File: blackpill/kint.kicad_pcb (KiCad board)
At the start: 2 copper layers, 99.9 x 86 mm, 17 parts, among them J1 RIGHT_THUMB, J2 LEFT_KEYWELL, J3 LEFT_FN_KEYS, J4 RIGHT_FN_KEYS, J7 RIGHT_KEYWELL, J8 LEFT_THUMB, U1 YAAJ_WeAct_BlackPill_Part_Lik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

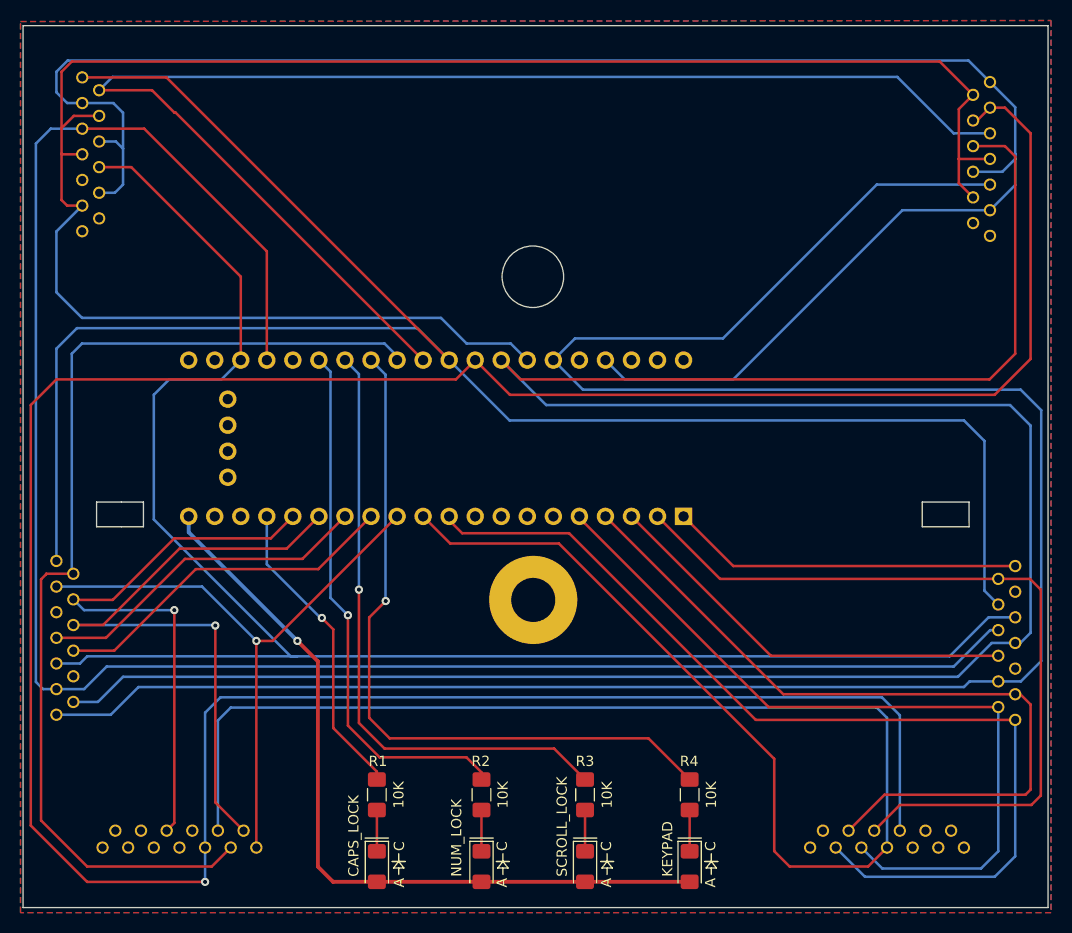
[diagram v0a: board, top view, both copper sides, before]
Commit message: Remove silkscreen writing area
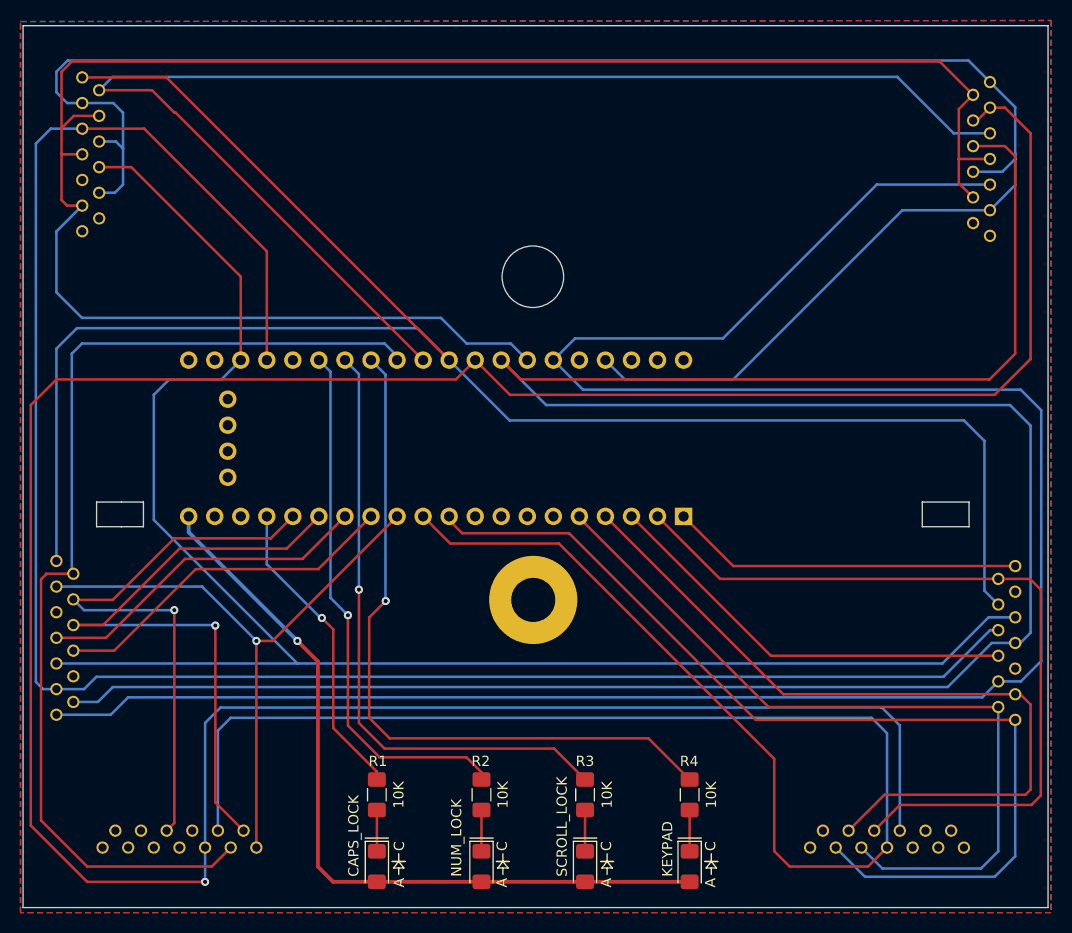
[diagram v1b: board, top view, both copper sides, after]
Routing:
- net /COL_6: track 155.0 -> 152.7 mm
- net /COL_5: track 288.1 -> 286.1 mm

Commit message: move tracks
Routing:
- net /LED_KEYPAD: track 69.9 -> 66.8 mm
- net /LED_SCROLL_LOCK: track 60.3 -> 58.8 mm
- net /ROW_3: track 56.8 -> 58.1 mm
- net /LED_NUM_LOCK: track 52.4 -> 51.9 mm
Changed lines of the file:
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@@
-	)
-	(segment
-		(start 113.5 119)
-		(end 113.5 139.75)
-		(width 0.25)
-		(layer "F.Cu")
-		(net 2)
 	)
 	(segment
@@
 	)
 	(segment
+		(start 114 139.25)
+		(end 112.75 140.5)
+		(width 0.25)
+		(layer "F.Cu")
+		(net 2)
+	)
+	(segment
 		(start 125.06 109.855)
 		(end 122.915 112)
@@
 	)
 	(segment
-		(start 113.5 139.75)
-		(end 112.75 140.5)
+		(start 114 118)
+		(end 114 139.25)
 		(width 0.25)
 		(layer "F.Cu")
@@
 	)
 	(via
-		(at 113.5 119)
+		(at 114 118)
 		(size 0.8)
 		(drill 0.4)
@@
 	)
 	(segment
-		(start 113.5 119)
-		(end 104.7 119)
-		(width 0.25)
-		(layer "B.Cu")
-		(net 2)
-	)
-	(segment
-		(start 104.7 119)
-		(end 103.65 117.95)
+		(start 114 118)
+		(end 103.7 118)
 		(width 0.25)
 		(layer "B.Cu")
@@
 	)
 	(segment
-		(start 107.642834 122.95)
+		(start 115 115)
+		(end 107.05 122.95)
+		(width 0.25)
+		(layer "F.Cu")
+		(net 22)
+	)
+	(segment
+		(start 127.535 115)
+		(end 115 115)
+		(width 0.25)
+		(layer "F.Cu")
+		(net 22)
+	)
+	(segment
+		(start 107.05 122.95)
 		(end 103.65 122.95)
 		(width 0.25)
@@
 	)
 	(segment
-		(start 127.535 115)
-		(end 115.592834 115)
-		(width 0.25)
-		(layer "F.Cu")
-		(net 22)
-	)
-	(segment
-		(start 115.592834 115)
-		(end 107.642834 122.95)
-		(width 0.25)
-		(layer "F.Cu")
-		(net 22)
-	)
-	(segment
-		(start 125.5 122)
-		(end 127.5 124)
-		(width 0.375)
-		(layer "F.Cu")
-		(net 24)
-	)
-	(segment
-		(start 127.5 144.01)
-		(end 128.9811 145.4911)
-		(width 0.375)
-		(layer "F.Cu")
-		(net 24)
-	)
-	(segment
-		(start 127.5 124)
-		(end 127.5 144.01)
+		(start 126 122.5)
+		(end 126 142.51)
 		(width 0.375)
 		(layer "F.Cu")
@@
 		(net 24)
 	)
+	(segment
+		(start 126 142.51)
+		(end 128.9811 145.4911)
+		(width 0.375)
+		(layer "F.Cu")
+		(net 24)
+	)
 	(via
-		(at 125.5 122)
+		(at 126 122.5)
 		(size 0.8)
 		(drill 0.4)
@@
 	)
 	(segment
+		(start 126 122.5)
+		(end 114.9 111.4)
+		(width 0.375)
+		(layer "B.Cu")
+		(net 24)
+	)
+	(segment
 		(start 114.9 111.4)
 		(end 114.9 109.855)
@@
 	)
 	(segment
-		(start 125.5 122)
-		(end 114.9 111.4)
-		(width 0.375)
-		(layer "B.Cu")
-		(net 24)
-	)
-	(segment
 		(start 158.08 109.855)
 		(end 171.675 123.45)
@@
 	)
 	(segment
-		(start 195.5 119.7)
-		(end 192.906544 119.7)
+		(start 192.3 119.7)
+		(end 195.5 119.7)
+		(width 0.25)
+		(layer "B.Cu")
+		(net 35)
+	)
+	(segment
+		(start 125.5 124.2)
+		(end 187.8 124.2)
 		(width 0.25)
 		(layer "B.Cu")
@@
 	)
 	(segment
-		(start 188.406544 124.2)
-		(end 125.5 124.2)
+		(start 187.8 124.2)
+		(end 192.3 119.7)
 		(width 0.25)
 		(layer "B.Cu")
@@
 		(start 111.5 98)
 		(end 111.5 110.2)
-		(width 0.25)
-		(layer "B.Cu")
-		(net 35)
-	)
-	(segment
-		(start 192.906544 119.7)
-		(end 188.406544 124.2)
 		(width 0.25)
 		(layer "B.Cu")
@@
 	)
 	(segment
-		(start 129 120.872)
-		(end 129 130.5)
-		(width 0.25)
-		(layer "F.Cu")
-		(net 48)
-	)
-	(segment
-		(start 129 130.5)
-		(end 133.2511 134.7511)
+		(start 127.25 120.25)
+		(end 127.25 128.75)
 		(width 0.25)
 		(layer "F.Cu")
@@
 	)
 	(segment
-		(start 127.889 119.761)
-		(end 129 120.872)
+		(start 127.25 128.75)
+		(end 133.2511 134.7511)
 		(width 0.25)
 		(layer "F.Cu")
@@
 	)
 	(via
-		(at 127.889 119.761)
+		(at 127.25 120.25)
 		(size 0.8)
 		(drill 0.4)
@@
 	)
 	(segment
-		(start 122.52 109.855)
-		(end 122.52 114.52)
+		(start 122.52 115.52)
+		(end 122.52 109.855)
 		(width 0.25)
 		(layer "B.Cu")
@@
 	)
 	(segment
-		(start 127.761 119.761)
-		(end 127.889 119.761)
+		(start 127.25 120.25)
+		(end 122.52 115.52)
 		(width 0.25)
 		(layer "B.Cu")
@@
 	)
 	(segment
-		(start 122.52 114.52)
-		(end 127.761 119.761)
-		(width 0.25)
-		(layer "B.Cu")
-		(net 48)
+		(start 143.4511 135.5161)
+		(end 143.4511 134.8151)
+		(width 0.25)
+		(layer "F.Cu")
+		(net 49)
+	)
+	(segment
+		(start 134.372659 133.35)
+		(end 128.7284 127.70574)
+		(width 0.25)
+		(layer "F.Cu")
+		(net 49)
+	)
+	(segment
+		(start 128.7284 127.70574)
+		(end 128.7284 118.5)
+		(width 0.25)
+		(layer "F.Cu")
+		(net 49)
 	)
 	(segment
 		(start 141.986 133.35)
-		(end 143.4511 134.8151)
+		(end 134.372659 133.35)
 		(width 0.25)
 		(layer "F.Cu")
@@
 	)
 	(segment
-		(start 133.518278 133.35)
+		(start 143.4511 134.8151)
 		(end 141.986 133.35)
 		(width 0.25)
@@
 		(net 49)
 	)
-	(segment
-		(start 130.429 130.260722)
-		(end 133.518278 133.35)
-		(width 0.25)
-		(layer "F.Cu")
-		(net 49)
-	)
-	(segment
-		(start 130.429 119.5)
-		(end 130.429 130.260722)
-		(width 0.25)
-		(layer "F.Cu")
-		(net 49)
-	)
-	(segment
-		(start 143.4511 134.8151)
-		(end 143.4511 135.5161)
-		(width 0.25)
-		(layer "F.Cu")
-		(net 49)
-	)
 	(via
-		(at 130.429 119.5)
+		(at 128.7284 118.5)
 		(size 0.8)
 		(drill 0.4)
@@
 	)
 	(segment
-		(start 128.7284 117.7994)
-		(end 130.429 119.5)
+		(start 128.7284 118.5)
+		(end 128.7284 95.7434)
 		(width 0.25)
 		(layer "B.Cu")
@@
 	)
 	(segment
-		(start 127.6 94.615)
-		(end 128.7284 95.7434)
+		(start 128.7284 95.7434)
+		(end 127.6 94.615)
 		(width 0.25)
 		(layer "B.Cu")
@@
 	)
 	(segment
-		(start 128.7284 95.7434)
-		(end 128.7284 117.7994)
-		(width 0.25)
-		(layer "B.Cu")
-		(net 49)
-	)
-	(segment
-		(start 134 132.5)
-		(end 150.535 132.5)
+		(start 131.5 117)
+		(end 131.5 127.5)
 		(width 0.25)
 		(layer "F.Cu")
@@
 	)
 	(segment
-		(start 131.5 117)
-		(end 131.5 130)
+		(start 131.5 127.5)
+		(end 136 132)
 		(width 0.25)
 		(layer "F.Cu")
@@
 	)
 	(segment
-		(start 150.535 132.5)
+		(start 150.035 132)
 		(end 153.5511 135.5161)
 		(width 0.25)
@@
 	)
 	(segment
-		(start 131.5 130)
-		(end 134 132.5)
+		(start 136 132)
+		(end 150.035 132)
 		(width 0.25)
 		(layer "F.Cu")
@@
 	)
 	(segment
-		(start 132.5 129.5)
-		(end 134.5 131.5)
+		(start 134.112 118.11)
+		(end 134.112 128.112)
 		(width 0.25)
 		(layer "F.Cu")
@@
 	)
 	(segment
-		(start 132.5 119.722)
-		(end 132.5 129.5)
+		(start 134.112 128.112)
+		(end 136.5 130.5)
 		(width 0.25)
 		(layer "F.Cu")
@@
 	)
 	(segment
-		(start 134.5 131.5)
-		(end 159.735 131.5)
+		(start 158.735 130.5)
+		(end 163.7511 135.5161)
 		(width 0.25)
 		(layer "F.Cu")
@@
 	)
 	(segment
-		(start 159.735 131.5)
-		(end 163.7511 135.5161)
-		(width 0.25)
-		(layer "F.Cu")
-		(net 51)
-	)
-	(segment
-		(start 134.112 118.11)
-		(end 132.5 119.722)
-		(width 0.25)
-		(layer "F.Cu")
+		(start 136.5 130.5)
+		(end 158.735 130.5)
+		(width 0.25)
+		(layer "F.Cu")
